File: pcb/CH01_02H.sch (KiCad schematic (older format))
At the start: 8 parts

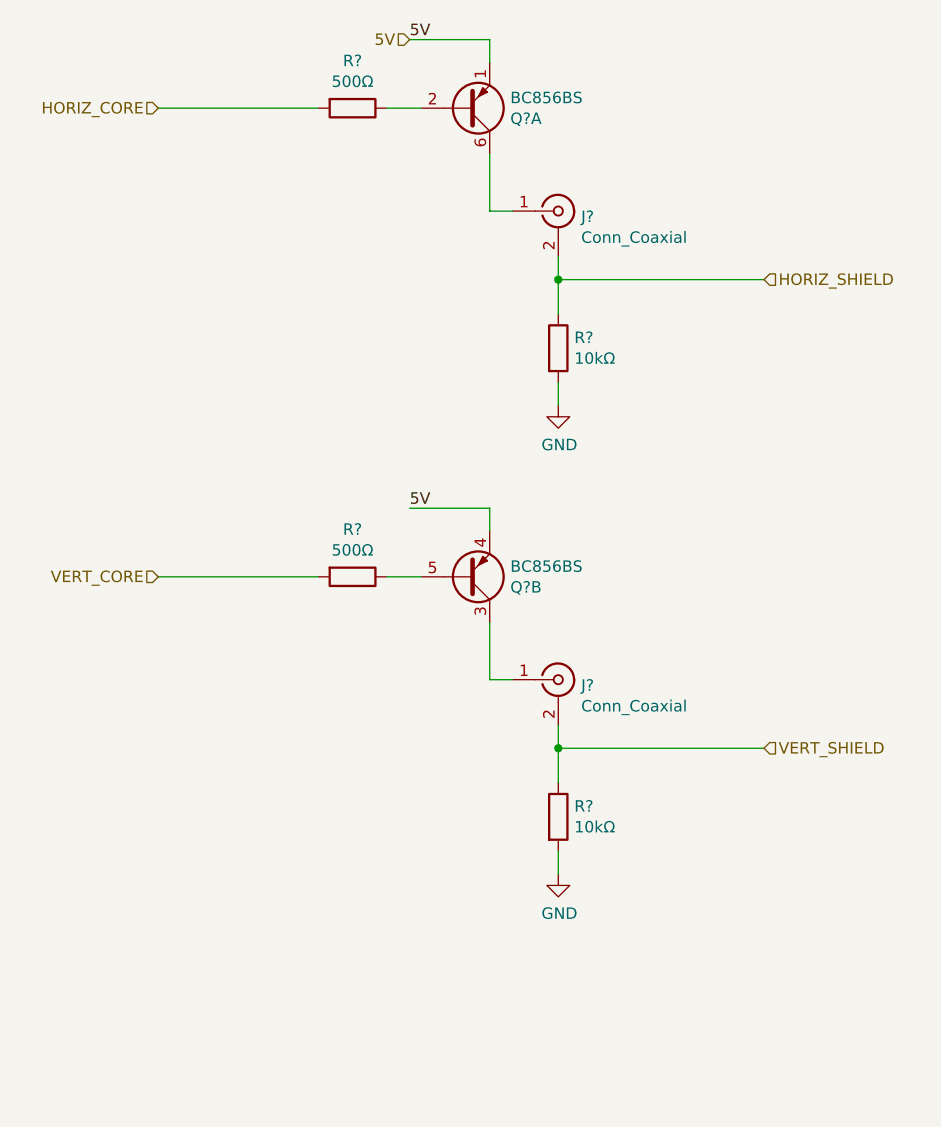
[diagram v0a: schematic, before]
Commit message: Completes first cut of the schematic
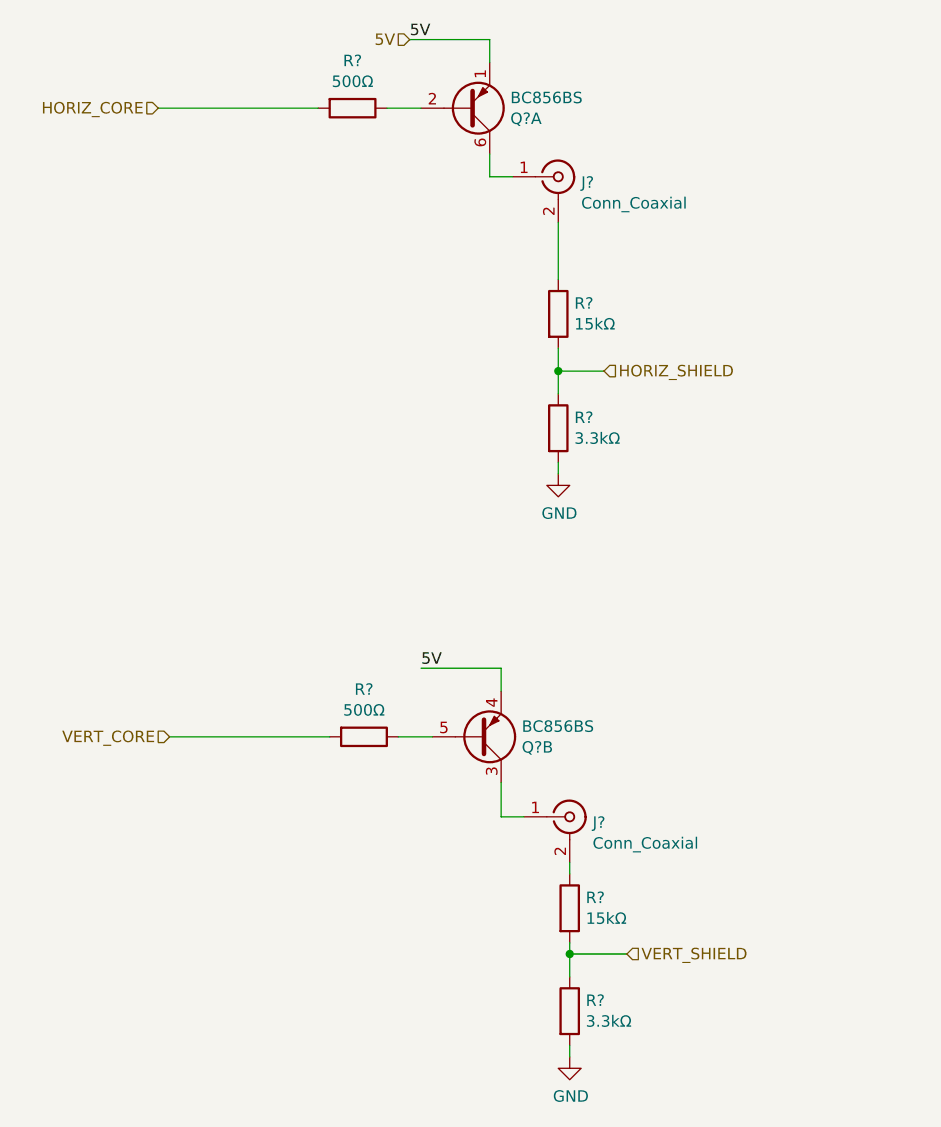
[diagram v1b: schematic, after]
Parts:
- removed R?: 10kΩ, Resistor_SMD:R_0805_2012Metric, symbol Device:R
- added R? (x2): 3.3kΩ, Resistor_SMD:R_0805_2012Metric, symbol Device:R
- added R?: 15kΩ, Resistor_SMD:R_0805_2012Metric, symbol Device:R
- R?: value 10kΩ -> 15kΩ
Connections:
- net GND: now also R?.2, R?.2; no longer R?.2
- net HORIZ_SHIELD: now also R?.2, R?.1; no longer J?.2 (Ext), R?.1
- net VERT_SHIELD: now also R?.1, R?.2; no longer J?.2 (Ext)
- new net: J?.2 (Ext), R?.1 (x2)
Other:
- moved on the sheet: J?, Q?B, R?
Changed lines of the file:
@@
 L Connector:Conn_Coaxial J?
 U 1 1 61B7F87D
-P 4600 2500
+P 4600 2350
 AR Path="/61B7F87D" Ref="J?"  Part="1"
 AR Path="/61B3F4A6/61B7F87D" Ref="J?"  Part="1"
 AR Path="/61B5B9BC/61B7F87D" Ref="J?"  Part="1"
 AR Path="/61C60B45/61C64A42/61B7F87D" Ref="J?"  Part="1"
-F 0 "J?" H 4700 2475 50  0000 L CNN
-F 1 "Conn_Coaxial" H 4700 2384 50  0000 L CNN
-F 2 "CoaxTester:FB_EPG" H 4600 2500 50  0001 C CNN
-F 3 " ~" H 4600 2500 50  0001 C CNN
-	1    4600 2500
+F 0 "J?" H 4700 2325 50  0000 L CNN
+F 1 "Conn_Coaxial" H 4700 2234 50  0000 L CNN
+F 2 "CoaxTester:FB_EPG" H 4600 2350 50  0001 C CNN
+F 3 " ~" H 4600 2350 50  0001 C CNN
+	1    4600 2350
 	1    0    0    -1
 $EndComp
@@
 L Device:R R?
 U 1 1 61B7F87F
-P 4600 3100
+P 4600 2950
 AR Path="/61B7F87F" Ref="R?"  Part="1"
 AR Path="/61B3F4A6/61B7F87F" Ref="R?"  Part="1"
 AR Path="/61B5B9BC/61B7F87F" Ref="R?"  Part="1"
 AR Path="/61C60B45/61C64A42/61B7F87F" Ref="R?"  Part="1"
-F 0 "R?" H 4670 3146 50  0000 L CNN
-F 1 "10kΩ" H 4670 3055 50  0000 L CNN
-F 2 "Resistor_SMD:R_0805_2012Metric" V 4530 3100 50  0001 C CNN
-F 3 "~" H 4600 3100 50  0001 C CNN
-	1    4600 3100
+F 0 "R?" H 4670 2996 50  0000 L CNN
+F 1 "15kΩ" H 4670 2905 50  0000 L CNN
+F 2 "Resistor_SMD:R_0805_2012Metric" V 4530 2950 50  0001 C CNN
+F 3 "~" H 4600 2950 50  0001 C CNN
+	1    4600 2950
 	1    0    0    -1
 $EndComp
 Wire Wire Line
-	4600 3250 4600 3350
-Wire Wire Line
-	4600 2700 4600 2800
-Wire Wire Line
-	4600 2800 5500 2800
-Connection ~ 4600 2800
-Wire Wire Line
-	4600 2800 4600 2950
+	4600 3600 4600 3650
+Wire Wire Line
+	4600 3200 4800 3200
 $Comp
 L Transistor_BJT:BC856BS Q?
@@
 $EndComp
 Wire Wire Line
-	4300 2250 4300 2500
-Wire Wire Line
-	4300 2500 4400 2500
+	4300 2250 4300 2350
+Wire Wire Line
+	4300 2350 4400 2350
 $Comp
 L power:GND #PWR?
 U 1 1 61B7F881
-P 4600 3350
+P 4600 3650
 AR Path="/61B7F881" Ref="#PWR?"  Part="1"
 AR Path="/61B3F4A6/61B7F881" Ref="#PWR?"  Part="1"
 AR Path="/61B5B9BC/61B7F881" Ref="#PWR?"  Part="1"
 AR Path="/61C60B45/61C64A42/61B7F881" Ref="#PWR?"  Part="1"
-F 0 "#PWR?" H 4600 3100 50  0001 C CNN
-F 1 "GND" H 4605 3177 50  0000 C CNN
-F 2 "" H 4600 3350 50  0001 C CNN
-F 3 "" H 4600 3350 50  0001 C CNN
-	1    4600 3350
+F 0 "#PWR?" H 4600 3400 50  0001 C CNN
+F 1 "GND" H 4605 3477 50  0000 C CNN
+F 2 "" H 4600 3650 50  0001 C CNN
+F 3 "" H 4600 3650 50  0001 C CNN
+	1    4600 3650
 	1    0    0    -1
 $EndComp
@@
 Text HLabel 3950 1750 0    50   Input ~ 0
 5V
-Text HLabel 5500 2800 2    50   Input ~ 0
+Text HLabel 4800 3200 2    50   Input ~ 0
 HORIZ_SHIELD
 $Comp
 L Connector:Conn_Coaxial J?
 U 1 1 61B7F882
-P 4600 4550
+P 4650 5150
 AR Path="/61B7F882" Ref="J?"  Part="1"
 AR Path="/61B3F4A6/61B7F882" Ref="J?"  Part="1"
 AR Path="/61B5B9BC/61B7F882" Ref="J?"  Part="1"
 AR Path="/61C60B45/61C64A42/61B7F882" Ref="J?"  Part="1"
-F 0 "J?" H 4700 4525 50  0000 L CNN
-F 1 "Conn_Coaxial" H 4700 4434 50  0000 L CNN
-F 2 "CoaxTester:FB_EPG" H 4600 4550 50  0001 C CNN
-F 3 " ~" H 4600 4550 50  0001 C CNN
-	1    4600 4550
+F 0 "J?" H 4750 5125 50  0000 L CNN
+F 1 "Conn_Coaxial" H 4750 5034 50  0000 L CNN
+F 2 "CoaxTester:FB_EPG" H 4650 5150 50  0001 C CNN
+F 3 " ~" H 4650 5150 50  0001 C CNN
+	1    4650 5150
 	1    0    0    -1
 $EndComp
@@
 L Device:R R?
 U 1 1 61B7F883
-P 3700 4100
+P 3750 4800
 AR Path="/61B7F883" Ref="R?"  Part="1"
 AR Path="/61B3F4A6/61B7F883" Ref="R?"  Part="1"
 AR Path="/61B5B9BC/61B7F883" Ref="R?"  Part="1"
 AR Path="/61C60B45/61C64A42/61B7F883" Ref="R?"  Part="1"
-F 0 "R?" V 3493 4100 50  0000 C CNN
-F 1 "500Ω" V 3584 4100 50  0000 C CNN
-F 2 "Resistor_SMD:R_0805_2012Metric" V 3630 4100 50  0001 C CNN
-F 3 "~" H 3700 4100 50  0001 C CNN
-	1    3700 4100
+F 0 "R?" V 3543 4800 50  0000 C CNN
+F 1 "500Ω" V 3634 4800 50  0000 C CNN
+F 2 "Resistor_SMD:R_0805_2012Metric" V 3680 4800 50  0001 C CNN
+F 3 "~" H 3750 4800 50  0001 C CNN
+	1    3750 4800
 	0    1    1    0
 $EndComp
 Wire Wire Line
-	2850 4100 3550 4100
-Wire Wire Line
-	3850 4100 4000 4100
-Wire Wire Line
-	4300 3900 4300 3800
-Wire Wire Line
-	4300 3800 3950 3800
-Text Label 3950 3800 0    50   ~ 0
+	2900 4800 3600 4800
+Wire Wire Line
+	3900 4800 4050 4800
+Wire Wire Line
+	4350 4600 4350 4500
+Wire Wire Line
+	4350 4500 4000 4500
+Text Label 4000 4500 0    50   ~ 0
 5V
-$Comp
-L Device:R R?
-U 1 1 61B7F884
-P 4600 5150
-AR Path="/61B7F884" Ref="R?"  Part="1"
-AR Path="/61B3F4A6/61B7F884" Ref="R?"  Part="1"
-AR Path="/61B5B9BC/61B7F884" Ref="R?"  Part="1"
-AR Path="/61C60B45/61C64A42/61B7F884" Ref="R?"  Part="1"
-F 0 "R?" H 4670 5196 50  0000 L CNN
-F 1 "10kΩ" H 4670 5105 50  0000 L CNN
-F 2 "Resistor_SMD:R_0805_2012Metric" V 4530 5150 50  0001 C CNN
-F 3 "~" H 4600 5150 50  0001 C CNN
-	1    4600 5150
-	1    0    0    -1
-$EndComp
-Wire Wire Line
-	4600 5300 4600 5400
-Wire Wire Line
-	4600 4750 4600 4850
-Wire Wire Line
-	4600 4850 5500 4850
-Connection ~ 4600 4850
-Wire Wire Line
-	4600 4850 4600 5000
+Wire Wire Line
+	4650 5750 4900 5750
 $Comp
 L Transistor_BJT:BC856BS Q?
 U 2 1 61B7F885
-P 4200 4100
+P 4250 4800
 AR Path="/61B7F885" Ref="Q?"  Part="1"
 AR Path="/61B3F4A6/61B7F885" Ref="Q?"  Part="2"
 AR Path="/61B5B9BC/61B7F885" Ref="Q?"  Part="1"
 AR Path="/61C60B45/61C64A42/61B7F885" Ref="Q?"  Part="2"
-F 0 "Q?" H 4390 4146 50  0000 L CNN
-F 1 "BC856BS" H 4390 4055 50  0000 L CNN
-F 2 "Package_TO_SOT_SMD:SOT-363_SC-70-6" H 4400 4200 50  0001 C CNN
-F 3 "https://assets.nexperia.com/documents/data-sheet/BC856BS.pdf" H 4200 4100 50  0001 C CNN
-	2    4200 4100
+F 0 "Q?" H 4440 4846 50  0000 L CNN
+F 1 "BC856BS" H 4440 4755 50  0000 L CNN
+F 2 "Package_TO_SOT_SMD:SOT-363_SC-70-6" H 4450 4900 50  0001 C CNN
+F 3 "https://assets.nexperia.com/documents/data-sheet/BC856BS.pdf" H 4250 4800 50  0001 C CNN
+	2    4250 4800
 	1    0    0    1
 $EndComp
 Wire Wire Line
-	4300 4300 4300 4550
-Wire Wire Line
-	4300 4550 4400 4550
-$Comp
-L power:GND #PWR?
-U 1 1 61B7F886
-P 4600 5400
-AR Path="/61B7F886" Ref="#PWR?"  Part="1"
-AR Path="/61B3F4A6/61B7F886" Ref="#PWR?"  Part="1"
-AR Path="/61B5B9BC/61B7F886" Ref="#PWR?"  Part="1"
-AR Path="/61C60B45/61C64A42/61B7F886" Ref="#PWR?"  Part="1"
-F 0 "#PWR?" H 4600 5150 50  0001 C CNN
-F 1 "GND" H 4605 5227 50  0000 C CNN
-F 2 "" H 4600 5400 50  0001 C CNN
-F 3 "" H 4600 5400 50  0001 C CNN
-	1    4600 5400
-	1    0    0    -1
-$EndComp
-Text HLabel 2850 4100 0    50   Input ~ 0
+	4350 5000 4350 5150
+Wire Wire Line
+	4350 5150 4450 5150
+Text HLabel 2900 4800 0    50   Input ~ 0
 VERT_CORE
-Text HLabel 5500 4850 2    50   Input ~ 0
+Text HLabel 4900 5750 2    50   Input ~ 0
 VERT_SHIELD
 $Bitmap
@@
 EndData
 $EndBitmap
+$Comp
+L Device:R R?
+U 1 1 61B6E486
+P 4600 3450
+AR Path="/61B6E486" Ref="R?"  Part="1"
+AR Path="/61B3F4A6/61B6E486" Ref="R?"  Part="1"
+AR Path="/61B5B9BC/61B6E486" Ref="R?"  Part="1"
+AR Path="/61C60B45/61C64A42/61B6E486" Ref="R?"  Part="1"
+F 0 "R?" H 4670 3496 50  0000 L CNN
+F 1 "3.3kΩ" H 4670 3405 50  0000 L CNN
+F 2 "Resistor_SMD:R_0805_2012Metric" V 4530 3450 50  0001 C CNN
+F 3 "~" H 4600 3450 50  0001 C CNN
+	1    4600 3450
+	1    0    0    -1
+$EndComp
+Wire Wire Line
+	4600 3100 4600 3200
+$Comp
+L Device:R R?
+U 1 1 61B6ED19
+P 4650 5550
+AR Path="/61B6ED19" Ref="R?"  Part="1"
+AR Path="/61B3F4A6/61B6ED19" Ref="R?"  Part="1"
+AR Path="/61B5B9BC/61B6ED19" Ref="R?"  Part="1"
+AR Path="/61C60B45/61C64A42/61B6ED19" Ref="R?"  Part="1"
+F 0 "R?" H 4720 5596 50  0000 L CNN
+F 1 "15kΩ" H 4720 5505 50  0000 L CNN
+F 2 "Resistor_SMD:R_0805_2012Metric" V 4580 5550 50  0001 C CNN
+F 3 "~" H 4650 5550 50  0001 C CNN
+	1    4650 5550
+	1    0    0    -1
+$EndComp
+Wire Wire Line
+	4650 6150 4650 6200
+$Comp
+L power:GND #PWR?
+U 1 1 61B6EE38
+P 4650 6200
+AR Path="/61B6EE38" Ref="#PWR?"  Part="1"
+AR Path="/61B3F4A6/61B6EE38" Ref="#PWR?"  Part="1"
+AR Path="/61B5B9BC/61B6EE38" Ref="#PWR?"  Part="1"
+AR Path="/61C60B45/61C64A42/61B6EE38" Ref="#PWR?"  Part="1"
+F 0 "#PWR?" H 4650 5950 50  0001 C CNN
+F 1 "GND" H 4655 6027 50  0000 C CNN
+F 2 "" H 4650 6200 50  0001 C CNN
+F 3 "" H 4650 6200 50  0001 C CNN
+	1    4650 6200
+	1    0    0    -1
+$EndComp
+$Comp
+L Device:R R?
+U 1 1 61B6EE42
+P 4650 6000
+AR Path="/61B6EE42" Ref="R?"  Part="1"
+AR Path="/61B3F4A6/61B6EE42" Ref="R?"  Part="1"
+AR Path="/61B5B9BC/61B6EE42" Ref="R?"  Part="1"
+AR Path="/61C60B45/61C64A42/61B6EE42" Ref="R?"  Part="1"
+F 0 "R?" H 4720 6046 50  0000 L CNN
+F 1 "3.3kΩ" H 4720 5955 50  0000 L CNN
+F 2 "Resistor_SMD:R_0805_2012Metric" V 4580 6000 50  0001 C CNN
+F 3 "~" H 4650 6000 50  0001 C CNN
+	1    4650 6000
+	1    0    0    -1
+$EndComp
+Wire Wire Line
+	4650 5700 4650 5750
+Wire Wire Line
+	4650 5350 4650 5400
+Wire Wire Line
+	4600 2550 4600 2800
+Connection ~ 4600 3200
+Wire Wire Line
+	4600 3200 4600 3300
+Connection ~ 4650 5750
+Wire Wire Line
+	4650 5750 4650 5850
 $EndSCHEMATC

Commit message: Updates schematic based on some testing. Adds PDF for review
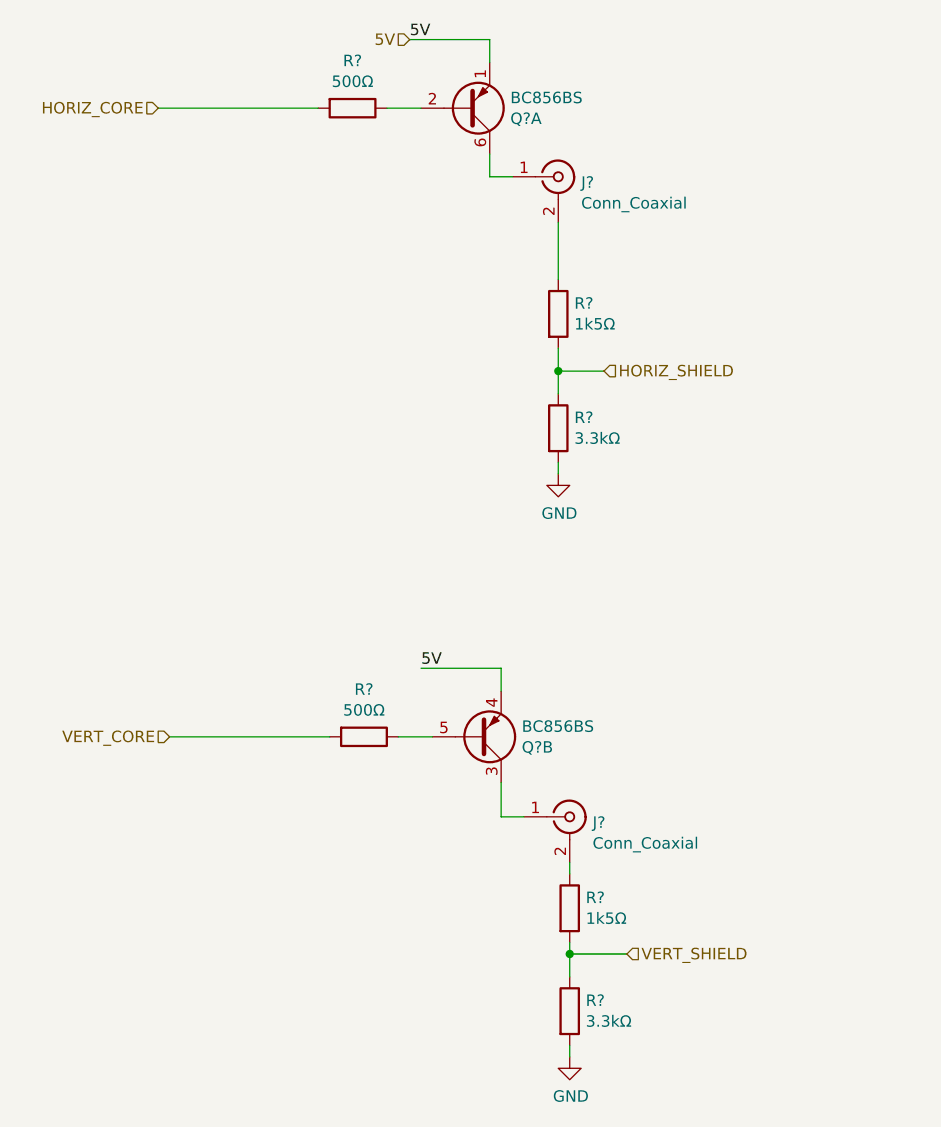
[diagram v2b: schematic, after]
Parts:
- R? (x2): value 15kΩ -> 1k5Ω
